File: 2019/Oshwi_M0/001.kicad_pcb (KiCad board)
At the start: 2 copper layers, 74.7 x 96.8 mm, 33 parts, among them SW1 SW_Push, U1 AP2112-3.3, U2 MCP73831T-2ACI/OT, U3 2MB Flash, X1 JSTPH, X2 32.768, X3 microUSB

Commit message: Update 3d Model
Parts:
- added REF**: MSOP-10_3x3mm_P0.5mm, Package_SO:MSOP-10_3x3mm_P0.5mm, F.Cu at (132.6, 50.0)

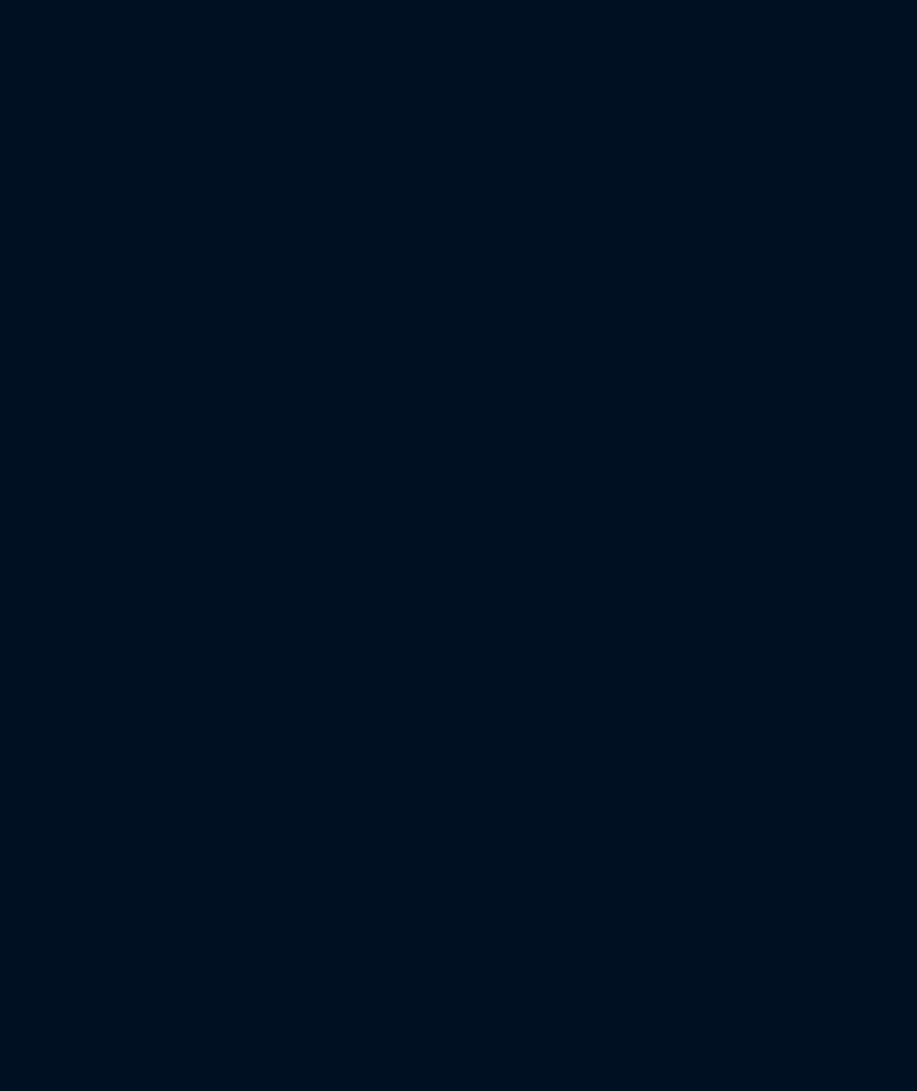
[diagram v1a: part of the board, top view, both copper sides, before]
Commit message: Add ESP32 Pico Docs
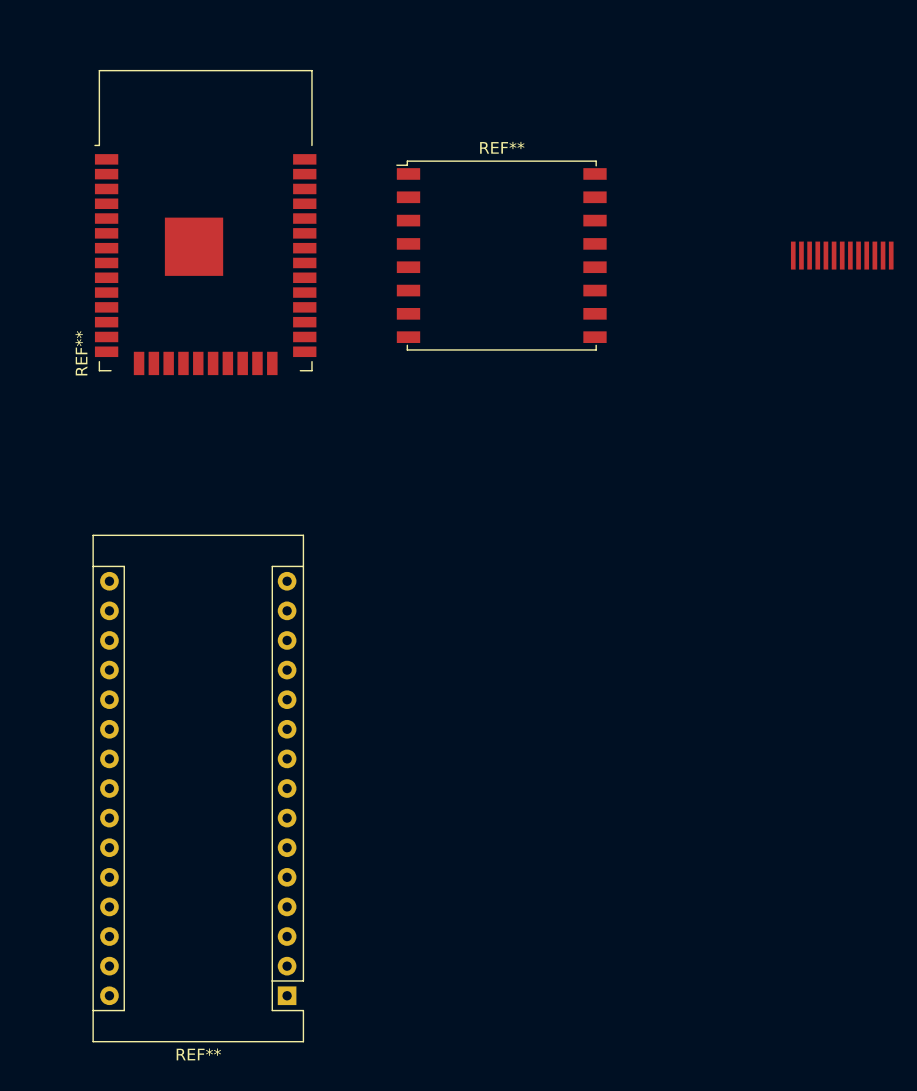
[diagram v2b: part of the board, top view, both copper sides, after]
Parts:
- added REF**: Arduino_Nano, Module:Arduino_Nano, F.Cu at (200.7, 142.2)
- added REF**: TFT_0.96_SPI, Display:TFT_0.96_SPI, F.Cu at (248.3, 78.7)
- added REF**: HOPERF_RFM9XW_SMD, RF_Module:HOPERF_RFM9XW_SMD, F.Cu at (219.1, 78.7)
- added REF**: ESP32-WROOM-32, RF_Module:ESP32-WROOM-32, F.Cu at (193.7, 78.7)
